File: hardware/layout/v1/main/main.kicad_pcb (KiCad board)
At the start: 4 copper layers, 41 x 56 mm, 52 parts, among them J1 12-32V DC In, J2 Crown board, J3 Probe board, J4 SEN55 PM, Q1 AO3400A, SW1 SERVICE, U1 SCT2400TVBR, U2 LM66100, U3 XIAO ESP32C6, U4 BMP581, U5 LSM6DS3TR-C, U6 AS3935-BQFT, U7 74AHCT1G125

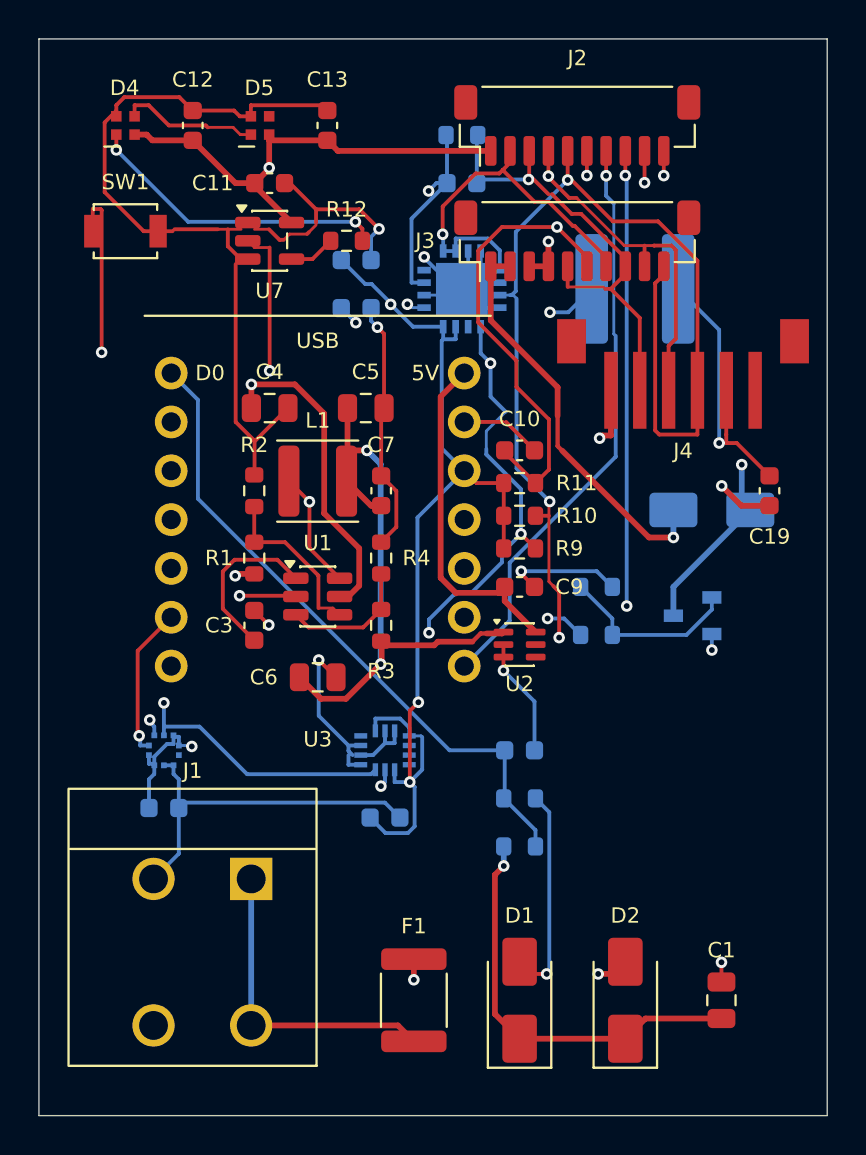
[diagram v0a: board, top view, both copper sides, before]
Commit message: Update project documentation and refactor crown sensor board circuit implementation
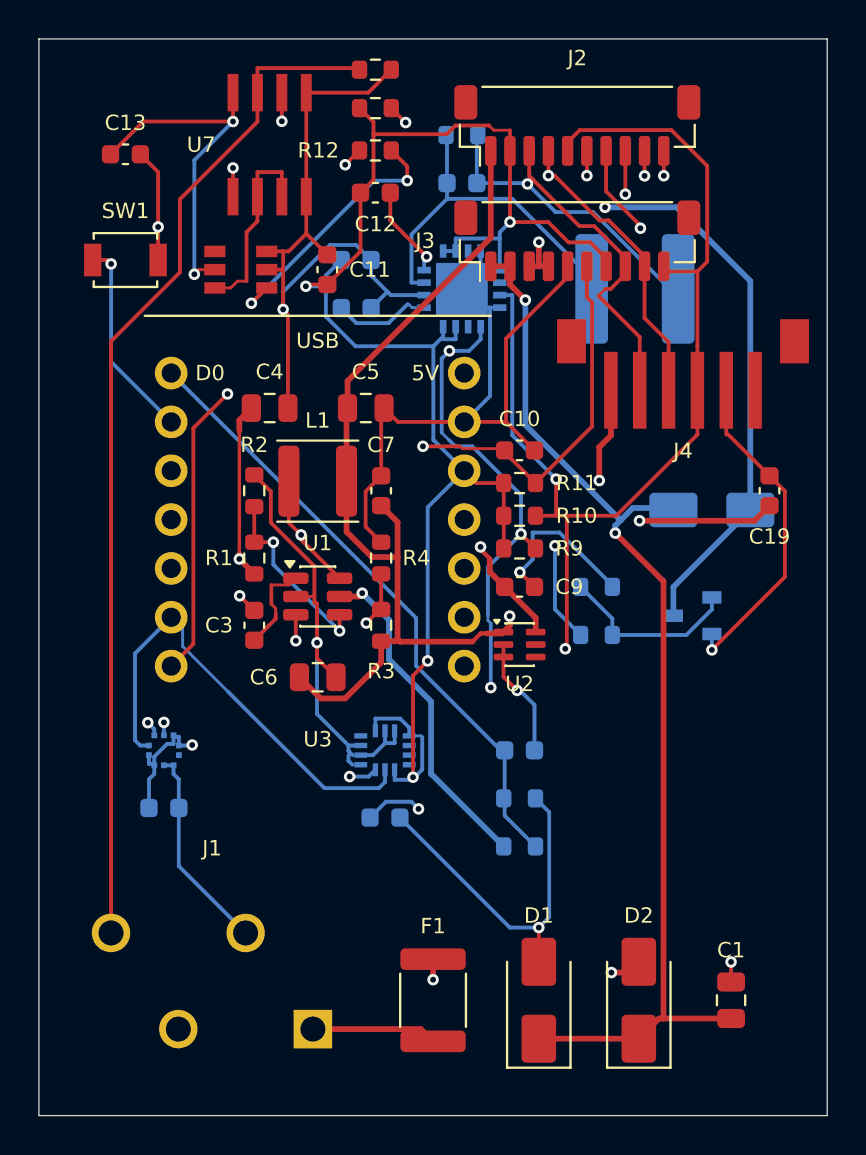
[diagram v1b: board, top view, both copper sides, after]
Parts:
- removed D4: RGB STATUS, gateway_fp:LED_SK6805-EC15_1.5x1.5mm
- removed D5: RGB WEATHER, gateway_fp:LED_SK6805-EC15_1.5x1.5mm
- added R14: 4k7, Resistor_SMD:R_0603_1608Metric, F.Cu at (17.5, -54.4)
- added R15: 10k, Resistor_SMD:R_0603_1608Metric, B.Cu at (22.0, -51.0)
- added U8: SN74LVC2G04DBVR, gateway_fp:TI_SN74LVC2G04_SOT-23-6, F.Cu at (10.5, -44.0)
- J1: value 12-32V DC In -> 12-32V + RS485; footprint gateway_fp:TerminalBlock_Kefa_KF142R-5.08-2P -> gateway_fp:TerminalBlock_Kefa_KF250-3.5-4P
- R12: value 330R -> 1k
- R13: value 10k -> 4k7; moved to F.Cu
- U7: value 74AHCT1G125 -> SP3485EN-L/TR; footprint Package_TO_SOT_SMD:SOT-23-5 -> gateway_fp:ON_LM393DR2G_SOIC-8
- moved C13 10.6 mm to (4.50, -50.0), turned to 0 degrees
- moved C12 10.1 mm to (17.5, -48.0), turned to 0 degrees
- moved C11 5.41 mm to (15.0, -44.0), turned to 90 degrees
- moved U7 5.00 mm to (12.0, -50.5)
- moved R12 4.93 mm to (17.5, -50.2)
- moved R13 4.71 mm to (17.5, -52.4)
- moved J1 1.58 mm to (9.00, -7.00)
- moved SW1 1.50 mm to (4.50, -44.5)
- moved D1 1.00 mm to (26.0, -6.00)
- moved F1 1.00 mm to (20.5, -6.00)
- moved D2 0.70 mm to (31.2, -6.00)
- moved C1 0.50 mm to (36.0, -6.00)
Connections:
- C11 pad 1: +5V -> +3V3
- C12 pad 1: +5V -> +3V3
- C13 pad 1: +5V -> +3V3
- R12 pad 1: N$1 -> RS485_RO
- R12 pad 2: N$2 -> RS485_IO
- R13 pad 1: AS_INP -> +3V3
- R13 pad 2: GND -> RS485_A
- U3 pad 11: LED_DATA -> RS485_IO
- U7 pad 1: GND -> RS485_RO
- U7 pad 2: LED_DATA -> RS485_DE
- U7 pad 3: GND -> RS485_DE
- U7 pad 4: N$1 -> GND
- U7 pad 5: +5V -> GND
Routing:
- net RS485_A: track 0.00 -> 62.0 mm, vias 0 -> 2
- net RS485_B: track 0.00 -> 53.5 mm
- net NTC_SENSE: track 82.8 -> 43.5 mm
- net +3V3: track 96.5 -> 135.7 mm, vias 5 -> 8
- net RS485_IO: track 0.00 -> 32.7 mm, vias 0 -> 2
- net GND: track 168.6 -> 199.2 mm, vias 13 -> 11
- net +5V: track 99.0 -> 71.0 mm, vias 5 -> 3
- net LED_DATA: track 21.0 -> 0.00 mm, vias 1 -> 0
- net N$2: track 15.9 -> 0.00 mm, vias 2 -> 0
- net US_RX: track 41.8 -> 27.7 mm
- net RS485_DE: track 0.00 -> 10.2 mm
- net VIN_RAW: track 16.4 -> 6.51 mm
- net I2C_SCL: track 92.9 -> 102.5 mm, vias 5 -> 2
- net VIN_PROT: track 119.5 -> 110.4 mm
- net HEAT_PWM: track 36.2 -> 27.7 mm
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
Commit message: Redesign crown PCB
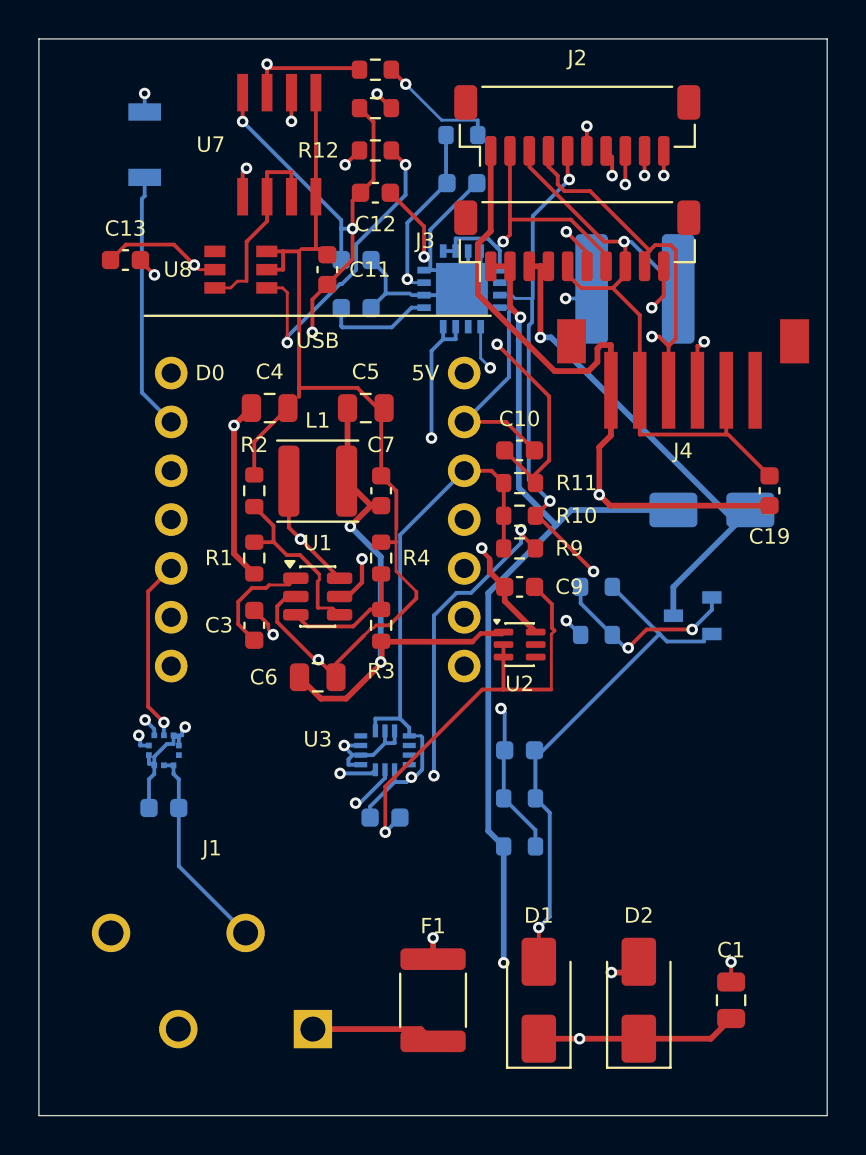
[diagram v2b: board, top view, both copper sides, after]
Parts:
- SW1: moved to B.Cu
- moved SW1 6.08 mm to (5.50, -50.5), turned to 90 degrees
- moved C13 5.50 mm to (4.50, -44.5)
- moved U7 0.50 mm to (12.5, -50.5)
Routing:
- net NTC_SENSE: track 43.5 -> 74.7 mm
- net US_TX: track 28.8 -> 48.2 mm
- net I2C_SCL: track 102.5 -> 86.9 mm, vias 2 -> 7
- net GND: track 199.2 -> 187.9 mm
- net HEAT_SW: track 34.7 -> 26.1 mm, vias 2 -> 1
- net +5V: track 71.0 -> 78.7 mm
- net VIN_PROT: track 110.4 -> 103.2 mm, vias 4 -> 5
- net VIN_ADC: track 33.0 -> 39.5 mm, vias 0 -> 1
- net US_RX: track 27.7 -> 34.0 mm
- net US_SEL_A: track 42.1 -> 47.7 mm, vias 2 -> 1
- net I2C_SDA: track 86.3 -> 82.6 mm
- net +3V3: track 135.7 -> 132.3 mm
- net RS485_IO: track 32.7 -> 29.7 mm
- net RAIN_ADC: track 39.1 -> 36.5 mm
- net BUCK5_FB: track 9.32 -> 6.91 mm, vias 2 -> 0
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
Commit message: Add silkscreen connector labels to all PCB variants for improved assembly identification
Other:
- board text added: "+V GND A+ B-"
- board text added: "CROWN"
- board text added: "PM"
- board text added: "PROBE"
- board text added: "RST"

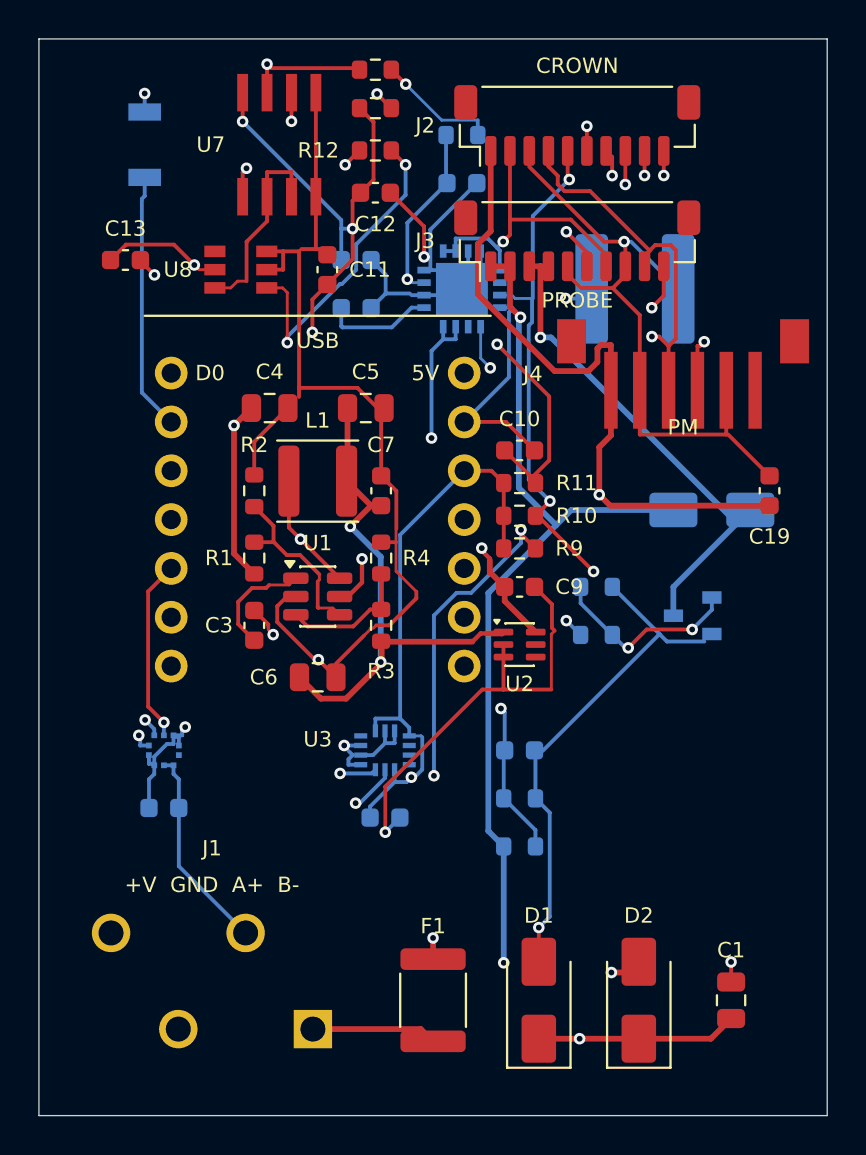
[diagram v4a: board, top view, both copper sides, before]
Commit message: Update enclosure dimensions, add power board, upgrade sensors, and redesign base bay for PMSA003I particulate module
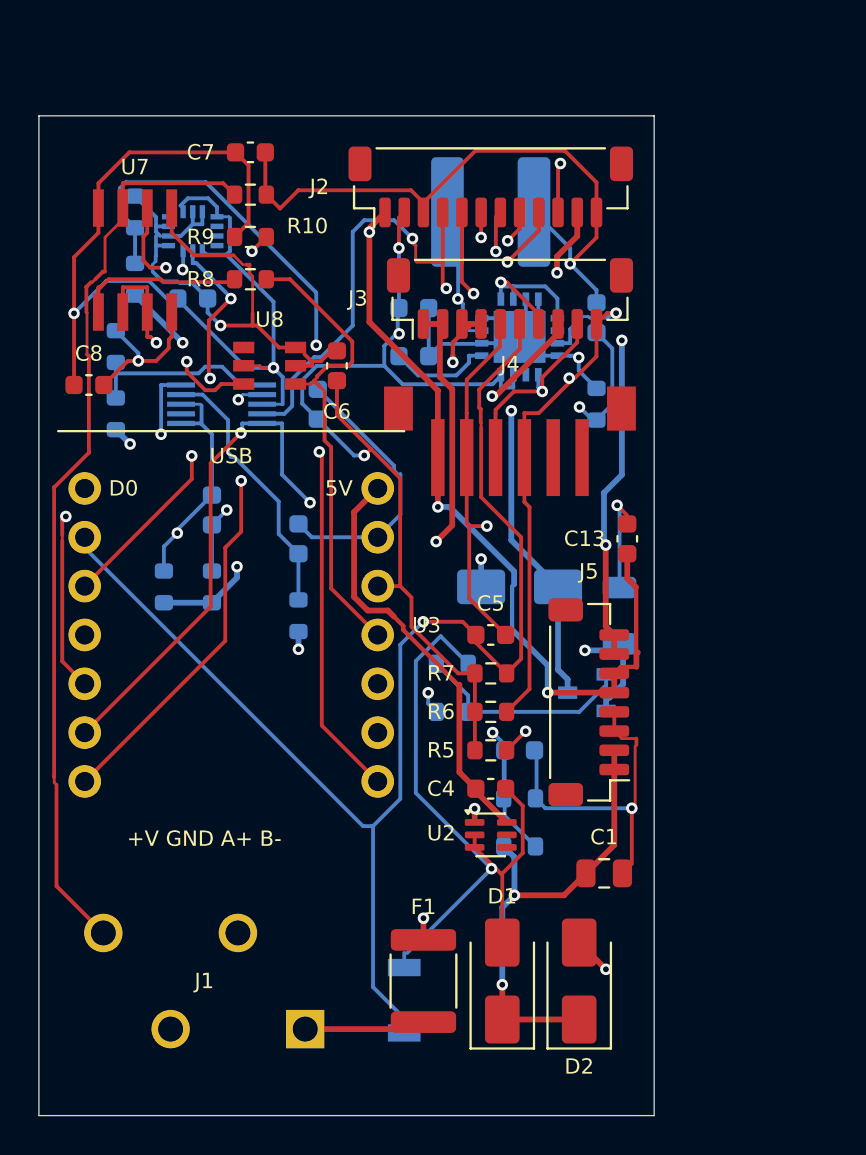
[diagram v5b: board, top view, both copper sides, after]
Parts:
- removed C14, C15, C17: 100n 50V, Capacitor_SMD:C_0603_1608Metric
- removed C16: 1u 50V, Capacitor_SMD:C_0603_1608Metric
- removed C18: 470p C0G 50V, Capacitor_SMD:C_0603_1608Metric
- removed L1: 4.7uH, Inductor_SMD:L_APV_ANR4012
- removed R12: 1k, Resistor_SMD:R_0603_1608Metric
- removed R13, R14: 4k7, Resistor_SMD:R_0603_1608Metric
- removed R15: 10k, Resistor_SMD:R_0603_1608Metric
- removed U1: SCT2400TVBR, Package_TO_SOT_SMD:TSOT-23-6
- added C20: 1u 50V, Capacitor_SMD:C_0603_1608Metric, B.Cu at (9.00, -31.5)
- added C21: 100n 50V, Capacitor_SMD:C_0603_1608Metric, B.Cu at (14.5, -37.0)
- added J5: Power board, Connector_JST:JST_SH_BM08B-SRSS-TB_1x08-1MP_P1.00mm_Vertical, F.Cu at (28.6, -21.5)
- added R16: 0R1, Resistor_SMD:R_1206_3216Metric, B.Cu at (30.2, -26.0)
- added R17: 1R, Resistor_SMD:R_0603_1608Metric, B.Cu at (6.50, -27.5)
- added R18: 1k, Resistor_SMD:R_0603_1608Metric, B.Cu at (13.5, -26.0)
- added R19: 1k, Resistor_SMD:R_0603_1608Metric, B.Cu at (9.00, -27.5)
- added R20: 10k, Resistor_SMD:R_0603_1608Metric, B.Cu at (4.00, -36.5)
- added R21: 10k, Resistor_SMD:R_0603_1608Metric, B.Cu at (4.00, -40.0)
- added R24: 10k, Resistor_SMD:R_0603_1608Metric, B.Cu at (5.00, -43.5)
- added R25: 10k, Resistor_SMD:R_0603_1608Metric, B.Cu at (5.00, -47.0)
- C10: value 100n 50V -> 1u 50V; moved to B.Cu
- C11, C3, R11, R2: moved to B.Cu
- C12: value 100n 50V -> 470p C0G 50V; moved to B.Cu
- C13: value 100n 50V -> 10u 10V
- C19: value 10u 10V -> 1u 50V; moved to B.Cu
- C4: value 10u 50V -> 10u 10V; footprint Capacitor_SMD:C_0805_2012Metric -> Capacitor_SMD:C_0603_1608Metric
- C5, C6: value 22u 25V -> 100n 50V; footprint Capacitor_SMD:C_0805_2012Metric -> Capacitor_SMD:C_0603_1608Metric
- C8: moved to F.Cu
- C9: value 10u 10V -> 100n 50V; moved to B.Cu
- J2: footprint Connector_JST:JST_SH_BM10B-SRSS-TB_1x10-1MP_P1.00mm_Vertical -> Connector_JST:JST_SH_BM12B-SRSS-TB_1x12-1MP_P1.00mm_Vertical
- J4: value SEN55 PM -> PMSA003I PM
- R1: value 51k -> 100k; moved to B.Cu
- R3: value 51k -> 330R; moved to B.Cu
- R4: value 10k -> 100k; moved to B.Cu
- R5: value 100k -> 4k7; moved to F.Cu
- R6: value 10k -> 4k7; moved to F.Cu
- R7: value 330R -> 10k; moved to F.Cu
- R8: value 100k -> 1k; moved to F.Cu
- U4: value BMP581 -> ADS1115IDGSR; footprint gateway_fp:Bosch_BMP581_LGA-10 -> gateway_fp:TI_ADS1115_VSSOP-10
- moved SW1 46.5 mm to (19.0, -6.00)
- moved C13 29.9 mm to (30.6, -30.0), turned to 90 degrees
- moved C8 29.4 mm to (2.60, -38.0)
- moved U5 28.8 mm to (8.00, -46.0)
- moved C19 24.6 mm to (13.5, -30.0)
- moved R8 24.1 mm to (11.0, -43.5)
- moved C4 22.9 mm to (23.5, -17.0)
- moved C9 22.7 mm to (8.00, -42.5)
- moved R10 21.8 mm to (11.0, -47.9)
- moved R9 21.4 mm to (11.0, -45.7)
- moved R2 21.1 mm to (25.0, -16.5), turned to 0 degrees
- moved R1 20.4 mm to (25.0, -14.0), turned to 0 degrees
- moved C7 18.9 mm to (11.0, -50.1), turned to 0 degrees
- moved U4 18.2 mm to (9.50, -37.0), turned to 90 degrees
- moved C6 16.2 mm to (15.5, -39.0), turned to 90 degrees
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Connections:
- C10 pad 1: NTC_SENSE -> AS_ACG
- C12 pad 1: +3V3 -> AS_INP
- C13 pad 1: +3V3 -> +5V
- C19 pad 1: +5V -> MON_REFL
- C3 pad 1: BUCK5_BST -> VIN_ADC
- C3 pad 2: BUCK5_SW -> GND
- C4 pad 1: VIN_PROT -> +5V_XIAO
- C5 pad 1: +5V -> NTC_SENSE
- C6 pad 1: +5V -> +3V3
- C7 pad 1: +5V -> +3V3
- C8 pad 1: VIN_ADC -> +3V3
- C9 pad 1: +5V_XIAO -> +3V3
- D3 pad 1: VIN_PROT -> +5V_HEAT
- J3 pad 1: VIN_PROT -> +5V_HEAT
- J3 pad 2: VIN_PROT -> +5V_HEAT
- J3 pad 8: GND -> CO2_HEAT_RTN
- J4 pad 5: GND -> (no net)
- Q1 pad 2: GND -> HEAT_SENSE
- R1 pad 2: BUCK5_EN -> VIN_ADC
- R10 pad 1: +3V3 -> RS485_B
- R10 pad 2: I2C_SCL -> GND
- R11 pad 1: +3V3 -> AS_INP
- R11 pad 2: NTC_SENSE -> GND
- R2 pad 1: BUCK5_EN -> VIN_ADC
- R3 pad 1: +5V -> HEAT_PWM
- R3 pad 2: BUCK5_FB -> HEAT_GATE
- R4 pad 1: BUCK5_FB -> HEAT_GATE
- R5 pad 1: VIN_PROT -> +3V3
- R5 pad 2: VIN_ADC -> I2C_SDA
- R6 pad 1: VIN_ADC -> +3V3
- R6 pad 2: GND -> I2C_SCL
- R7 pad 1: HEAT_PWM -> +3V3
- R7 pad 2: HEAT_GATE -> NTC_SENSE
- R8 pad 1: HEAT_GATE -> RS485_RO
- R8 pad 2: GND -> RS485_IO
- R9 pad 2: I2C_SDA -> RS485_A
- U4 pad 1: +3V3 -> GND
- U4 pad 10: +3V3 -> I2C_SCL
- U4 pad 2: I2C_SCL -> (no net)
- U4 pad 4: I2C_SDA -> MON_REFL
- U4 pad 5: +3V3 -> MON_PROBE
- U4 pad 6: +3V3 -> MON_5V
- U4 pad 7: (no net) -> MON_5V_LOGIC
- U4 pad 8: GND -> +3V3
- U4 pad 9: GND -> I2C_SDA
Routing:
- net VIN_PROT: track 103.2 -> 24.7 mm, vias 5 -> 2
- net +5V_HEAT: track 0.00 -> 71.9 mm, vias 0 -> 6
- net I2C_SDA: track 82.6 -> 114.7 mm
- net CO2_HEAT_RTN: track 0.00 -> 27.4 mm, vias 0 -> 2
- net MON_5V_LOGIC: track 0.00 -> 26.3 mm, vias 0 -> 2
- net HEAT_SENSE: track 0.00 -> 23.7 mm, vias 0 -> 2
- net MON_REFL: track 0.00 -> 14.0 mm
- net BUCK5_SW: track 13.4 -> 0.00 mm, vias 2 -> 0
- net +5V: track 78.7 -> 65.4 mm, vias 3 -> 5
- net MON_PROBE: track 0.00 -> 12.4 mm, vias 0 -> 2
- net MON_5V: track 0.00 -> 10.00 mm
- net I2C_SCL: track 86.9 -> 96.8 mm
- net BUCK5_EN: track 9.39 -> 0.00 mm
- net US_RX: track 34.0 -> 43.0 mm
- net US_SEL_A: track 47.7 -> 38.8 mm, vias 1 -> 2
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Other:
- board size 41 x 56 mm -> 32 x 52 mm
